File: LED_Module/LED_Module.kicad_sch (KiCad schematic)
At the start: 41 parts, among them J1 Conn_02x05_Odd_Even, J2 Conn_01x03_Male, J3 ESP8266 Header, SW1 SW_Push, SW2 SW_Push, U1 LD1117S33TR_SOT223, U2 STM32F091RCTx, U3 TPS62A02DRL, U4 24AA32AF EEPROM

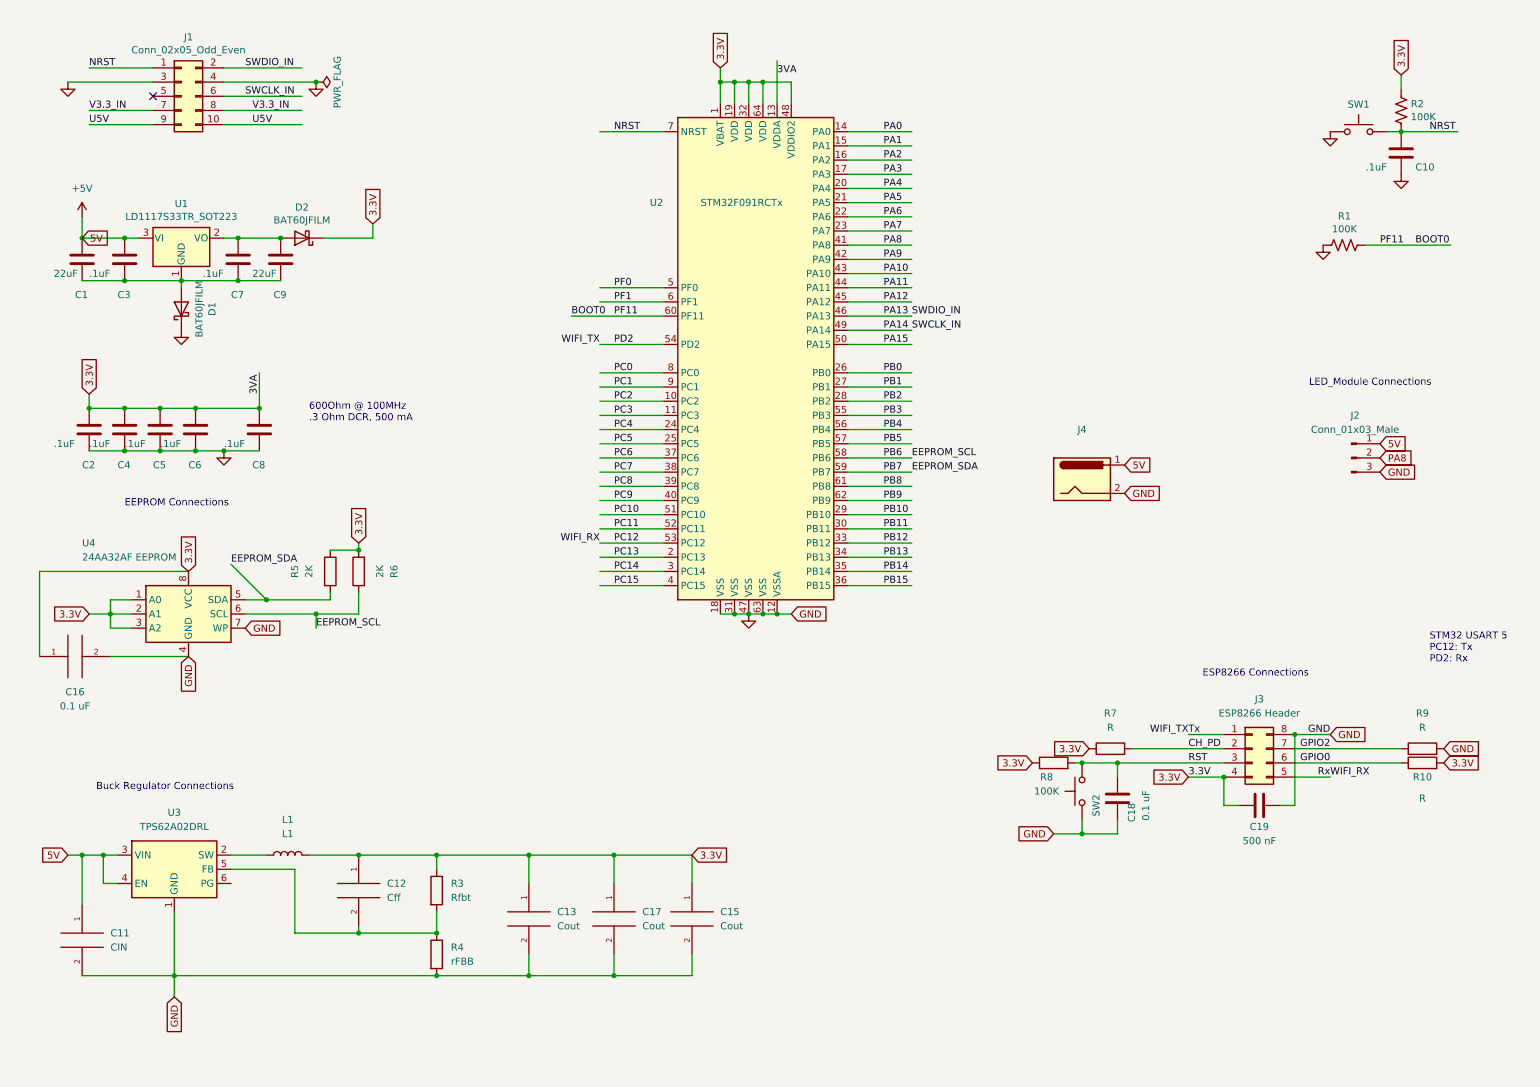
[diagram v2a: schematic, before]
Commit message: Revision to Buck Layout
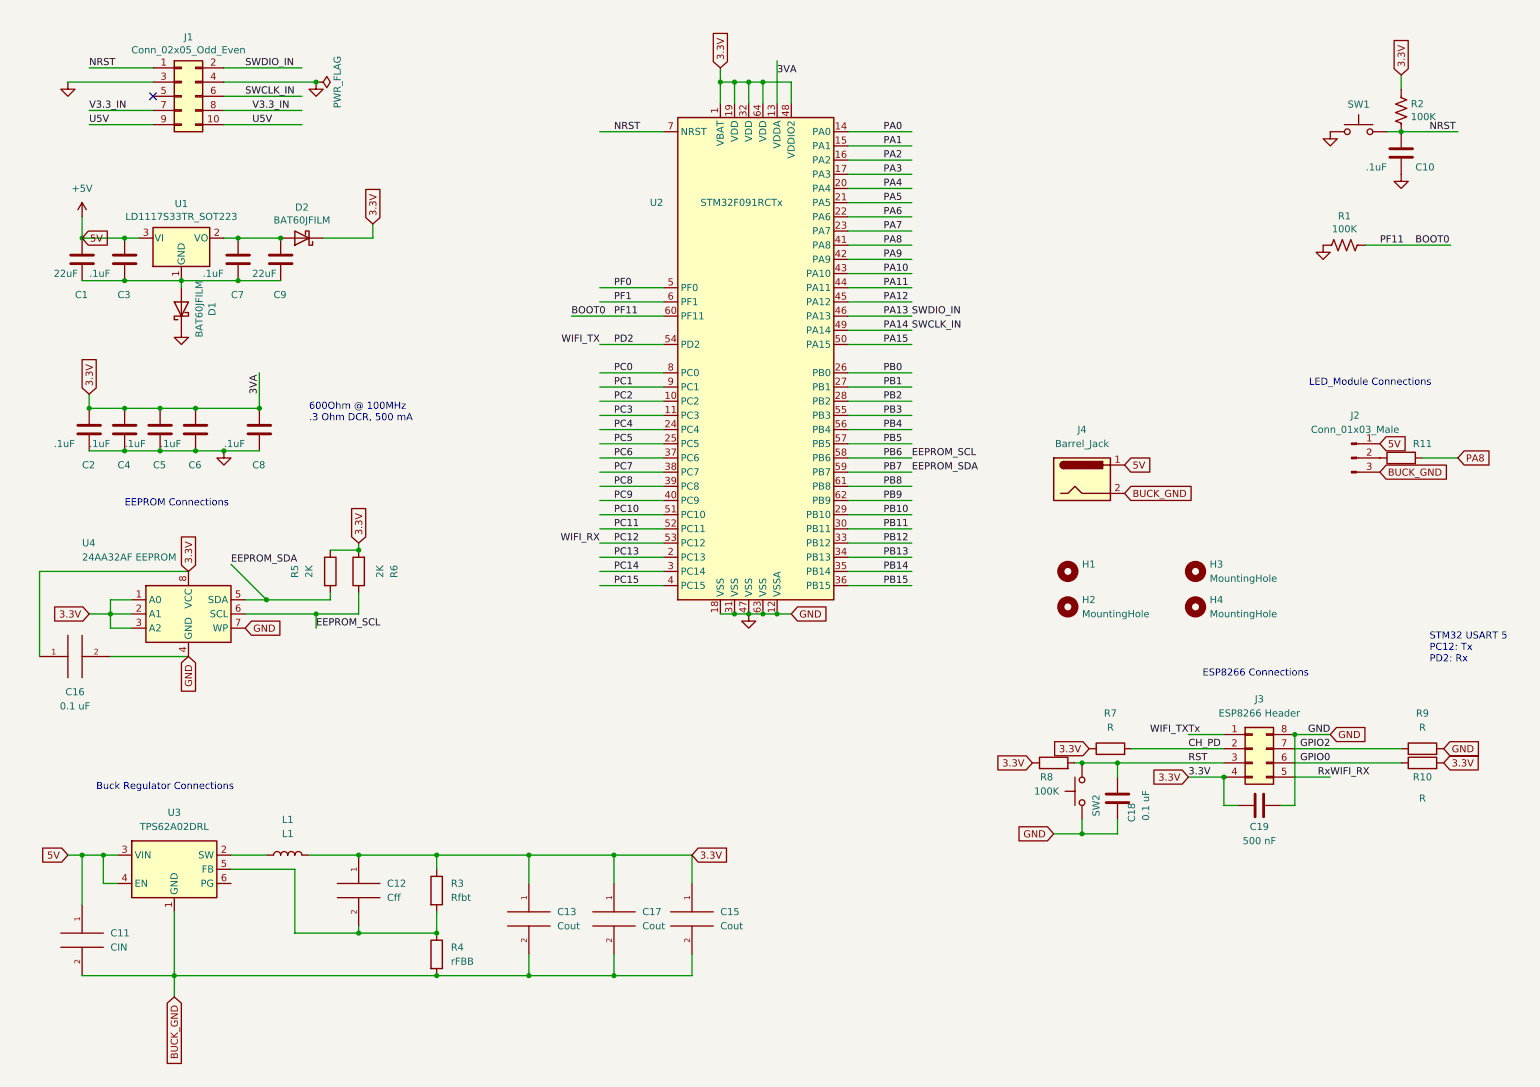
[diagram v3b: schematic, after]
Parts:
- added H1: (no value), symbol Mechanical:MountingHole
- added H2, H4: MountingHole, MountingHole:MountingHole_3.2mm_M3, symbol Mechanical:MountingHole
- added H3: MountingHole, symbol Mechanical:MountingHole
- added R11: (no value), symbol Device:R
- J4: value (none) -> Barrel_Jack; footprint (none) -> Connector_PinHeader_2.54mm:PinHeader_1x02_P2.54mm_Vertical
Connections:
- net GND: no longer C11.2, C13.2, C15.2, C17.2, J2.3 (Pin_3), J4.2, R4.2, U3.1 (GND)
- net PA8: now also R11.2; no longer J2.2 (Pin_2)
- new net: J2.2 (Pin_2), R11.1
- new net BUCK_GND: C11.2, C13.2, C15.2, C17.2, J2.3 (Pin_3), J4.2, R4.2, U3.1 (GND)
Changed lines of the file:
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@@
+    (stroke (width 0) (type default) (color 0 0 0 0))
+  )
+  (wire (pts (xy 265.43 92.71) (xy 271.78 92.71))
     (stroke (width 0) (type default) (color 0 0 0 0))
   )
@@
     )
   )
-  (global_label "PA8" (shape input) (at 257.81 92.71 0) (fields_autoplaced)
-    (effects (font (size 1.27 1.27)) (justify left))
-    (property "Intersheet References" "${INTERSHEET_REFS}" (id 0) (at 263.7912 92.6306 0)
+  (global_label "PA8" (shape input) (at 271.78 92.71 0) (fields_autoplaced)
+    (effects (font (size 1.27 1.27)) (justify left))
+    (property "Intersheet References" "${INTERSHEET_REFS}" (id 0) (at 277.7612 92.6306 0)
       (effects (font (size 1.27 1.27)) (justify left) hide)
     )
@@
     )
   )
-  (global_label "GND" (shape input) (at 212.09 99.06 0) (fields_autoplaced)
-    (effects (font (size 1.27 1.27)) (justify left))
-    (property "Intersheet References" "${INTERSHEET_REFS}" (id 0) (at 218.3736 98.9806 0)
+  (global_label "BUCK_GND" (shape input) (at 212.09 99.06 0) (fields_autoplaced)
+    (effects (font (size 1.27 1.27)) (justify left))
+    (property "Intersheet References" "${INTERSHEET_REFS}" (id 0) (at 224.4817 98.9806 0)
       (effects (font (size 1.27 1.27)) (justify left) hide)
     )
@@
     )
   )
-  (global_label "GND" (shape input) (at 41.91 189.23 270) (fields_autoplaced)
+  (global_label "BUCK_GND" (shape input) (at 41.91 189.23 270) (fields_autoplaced)
     (effects (font (size 1.27 1.27)) (justify right))
-    (property "Intersheet References" "${INTERSHEET_REFS}" (id 0) (at 41.9894 195.5136 90)
-      (effects (font (size 1.27 1.27)) (justify left) hide)
+    (property "Intersheet References" "${INTERSHEET_REFS}" (id 0) (at 41.8306 201.6217 90)
+      (effects (font (size 1.27 1.27)) (justify right) hide)
     )
   )
@@
     )
   )
-  (global_label "GND" (shape input) (at 257.81 95.25 0) (fields_autoplaced)
-    (effects (font (size 1.27 1.27)) (justify left))
-    (property "Intersheet References" "${INTERSHEET_REFS}" (id 0) (at 264.0936 95.1706 0)
+  (global_label "BUCK_GND" (shape input) (at 257.81 95.25 0) (fields_autoplaced)
+    (effects (font (size 1.27 1.27)) (justify left))
+    (property "Intersheet References" "${INTERSHEET_REFS}" (id 0) (at 270.2017 95.1706 0)
       (effects (font (size 1.27 1.27)) (justify left) hide)
     )
@@
     (pin "2")
   )
+  (symbol (lib_id "Mechanical:MountingHole") (at 224.79 119.38 0) (unit 1)
+    (in_bom yes) (on_board yes) (fields_autoplaced)
+    (property "Reference" "H4" (id 0) (at 227.33 118.1099 0)
+      (effects (font (size 1.27 1.27)) (justify left))
+    )
+    (property "Value" "MountingHole" (id 1) (at 227.33 120.6499 0)
+      (effects (font (size 1.27 1.27)) (justify left))
+    )
+    (property "Footprint" "MountingHole:MountingHole_3.2mm_M3" (id 2) (at 224.79 119.38 0)
+      (effects (font (size 1.27 1.27)) hide)
+    )
+    (property "Datasheet" "~" (id 3) (at 224.79 119.38 0)
+      (effects (font (size 1.27 1.27)) hide)
+    )
+  )
   (symbol (lib_id "Device:C") (at 26.67 87.63 0) (unit 1)
     (in_bom yes) (on_board yes)
@@
     (pin "2")
   )
+  (symbol (lib_id "Mechanical:MountingHole") (at 201.93 119.38 0) (unit 1)
+    (in_bom yes) (on_board yes) (fields_autoplaced)
+    (property "Reference" "H2" (id 0) (at 204.47 118.1099 0)
+      (effects (font (size 1.27 1.27)) (justify left))
+    )
+    (property "Value" "MountingHole" (id 1) (at 204.47 120.6499 0)
+      (effects (font (size 1.27 1.27)) (justify left))
+    )
+    (property "Footprint" "MountingHole:MountingHole_3.2mm_M3" (id 2) (at 201.93 119.38 0)
+      (effects (font (size 1.27 1.27)) hide)
+    )
+    (property "Datasheet" "~" (id 3) (at 201.93 119.38 0)
+      (effects (font (size 1.27 1.27)) hide)
+    )
+  )
   (symbol (lib_id "power:GND") (at 43.18 69.85 0) (unit 1)
     (in_bom yes) (on_board yes)
@@
     (pin "1")
   )
+  (symbol (lib_id "Mechanical:MountingHole") (at 201.93 113.03 0) (unit 1)
+    (in_bom yes) (on_board yes) (fields_autoplaced)
+    (property "Reference" "H1" (id 0) (at 204.47 111.7599 0)
+      (effects (font (size 1.27 1.27)) (justify left))
+    )
+    (property "Value" "" (id 1) (at 204.47 114.2999 0)
+      (effects (font (size 1.27 1.27)) (justify left))
+    )
+    (property "Footprint" "" (id 2) (at 201.93 113.03 0)
+      (effects (font (size 1.27 1.27)) hide)
+    )
+    (property "Datasheet" "~" (id 3) (at 201.93 113.03 0)
+      (effects (font (size 1.27 1.27)) hide)
+    )
+  )
   (symbol (lib_id "pspice:CAP") (at 25.4 179.07 0) (unit 1)
     (in_bom yes) (on_board yes) (fields_autoplaced)
@@
     )
     (property "Datasheet" "~" (id 3) (at 88.9 181.61 0)
+      (effects (font (size 1.27 1.27)) hide)
+    )
+    (pin "1")
+    (pin "2")
+  )
+  (symbol (lib_id "Device:R") (at 261.62 92.71 90) (unit 1)
+    (in_bom yes) (on_board yes)
+    (property "Reference" "R11" (id 0) (at 265.43 90.17 90))
+    (property "Value" "" (id 1) (at 265.43 92.71 90))
+    (property "Footprint" "" (id 2) (at 261.62 94.488 90)
+      (effects (font (size 1.27 1.27)) hide)
+    )
+    (property "Datasheet" "~" (id 3) (at 261.62 92.71 0)
       (effects (font (size 1.27 1.27)) hide)
     )
@@
     (pin "1")
   )
+  (symbol (lib_id "Mechanical:MountingHole") (at 224.79 113.03 0) (unit 1)
+    (in_bom yes) (on_board yes) (fields_autoplaced)
+    (property "Reference" "H3" (id 0) (at 227.33 111.7599 0)
+      (effects (font (size 1.27 1.27)) (justify left))
+    )
+    (property "Value" "MountingHole" (id 1) (at 227.33 114.2999 0)
+      (effects (font (size 1.27 1.27)) (justify left))
+    )
+    (property "Footprint" "" (id 2) (at 224.79 113.03 0)
+      (effects (font (size 1.27 1.27)) hide)
+    )
+    (property "Datasheet" "~" (id 3) (at 224.79 113.03 0)
+      (effects (font (size 1.27 1.27)) hide)
+    )
+  )
   (symbol (lib_id "pspice:CAP") (at 24.13 128.27 90) (unit 1)
     (in_bom yes) (on_board yes)
@@
     (in_bom yes) (on_board yes) (fields_autoplaced)
     (property "Reference" "J4" (id 0) (at 204.47 87.63 0))
-    (property "Value" "" (id 1) (at 204.47 90.17 0))
-    (property "Footprint" "" (id 2) (at 205.74 97.536 0)
+    (property "Value" "Barrel_Jack" (id 1) (at 204.47 90.17 0))
+    (property "Footprint" "Connector_PinHeader_2.54mm:PinHeader_1x02_P2.54mm_Vertical" (id 2) (at 205.74 97.536 0)
       (effects (font (size 1.27 1.27)) hide)
     )
@@
       (reference "D2") (unit 1) (value "BAT60JFILM") (footprint "Diode_SMD:D_SOD-323")
     )
+    (path "/6db4c715-f604-4ad5-b3e6-77e085153a04"
+      (reference "H1") (unit 1) (value "MountingHole") (footprint "MountingHole:MountingHole_3.2mm_M3")
+    )
+    (path "/622b77b6-409c-43f6-9eed-dd8b04a79249"
+      (reference "H2") (unit 1) (value "MountingHole") (footprint "MountingHole:MountingHole_3.2mm_M3")
+    )
+    (path "/d204374d-427d-4184-8cac-34c3c45ae776"
+      (reference "H3") (unit 1) (value "MountingHole") (footprint "MountingHole:MountingHole_3.2mm_M3")
+    )
+    (path "/59398cac-fd77-444e-9c8c-50373aefc347"
+      (reference "H4") (unit 1) (value "MountingHole") (footprint "MountingHole:MountingHole_3.2mm_M3")
+    )
     (path "/c7c34d7a-e4e9-4020-9eb2-3f57bf5616f3"
       (reference "J1") (unit 1) (value "Conn_02x05_Odd_Even") (footprint "Connector_IDC:IDC-Header_2x05_P2.54mm_Vertical")
@@
       (reference "R10") (unit 1) (value "R") (footprint "Resistor_SMD:R_0805_2012Metric_Pad1.20x1.40mm_HandSolder")
     )
+    (path "/76abd028-2505-456e-9c1d-86a704fa9431"
+      (reference "R11") (unit 1) (value "R") (footprint "Resistor_SMD:R_0805_2012Metric_Pad1.20x1.40mm_HandSolder")
+    )
     (path "/83a0af08-0788-496b-b5a2-dc27514fcb3a"

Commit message: Systems laid out and 3.3V connected
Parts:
- removed R9: R, Resistor_SMD:R_0805_2012Metric_Pad1.20x1.40mm_HandSolder, symbol Device:R
- added D3, D4, D6: LED, LED_SMD:LED_0805_2012Metric_Pad1.15x1.40mm_HandSolder, symbol Device:LED
- added D5: (no value), symbol Device:LED
- added R12, R14, R9: 3K, Resistor_SMD:R_0805_2012Metric_Pad1.20x1.40mm_HandSolder, symbol Device:R_US
- added R13: (no value), symbol Device:R_US
- SW2: footprint Button_Switch_SMD:SW_SPST_PTS645 -> (none)
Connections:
- net 3.3V: now also J3.7 (3.3V); no longer J3.4 (3.3V)
- net CH_PD: now also J3.3 (CH_PD); no longer J3.2 (CH_PD)
- net GND: now also J3.2 (GND), D3.1 (K), D4.1 (K), D5.1 (K), D6.1 (K); no longer J3.8 (GND)
- net GPIO2: no longer J3.7 (GPIO2)
- net PC12: now also J3.8 (Rx); no longer J3.5 (Rx)
- net PC6: now also R9.2
- net PC7: now also R12.2
- net PC8: now also R13.2
- net PC9: now also R14.2
- net RST: now also J3.5 (RST); no longer J3.3 (RST)
- new net: D6.2 (A), R14.1
- new net: D5.2 (A), R13.1
- new net: D3.2 (A), R9.1
- new net: D4.2 (A), R12.1
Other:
- moved on the sheet: J2, R11

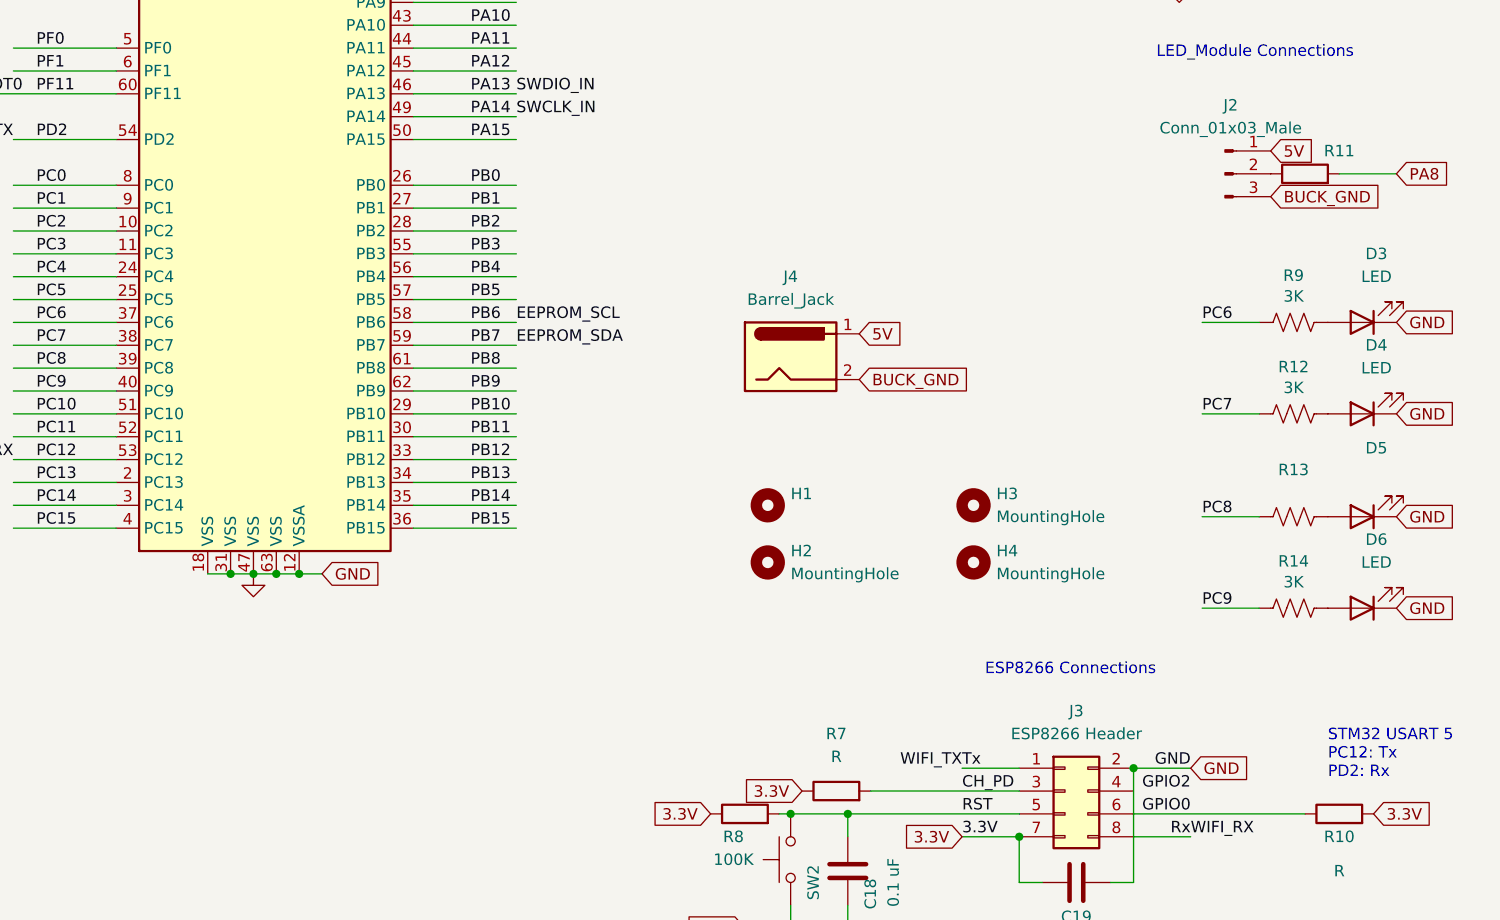
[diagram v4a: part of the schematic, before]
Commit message: Power and ground planes plus complete routing
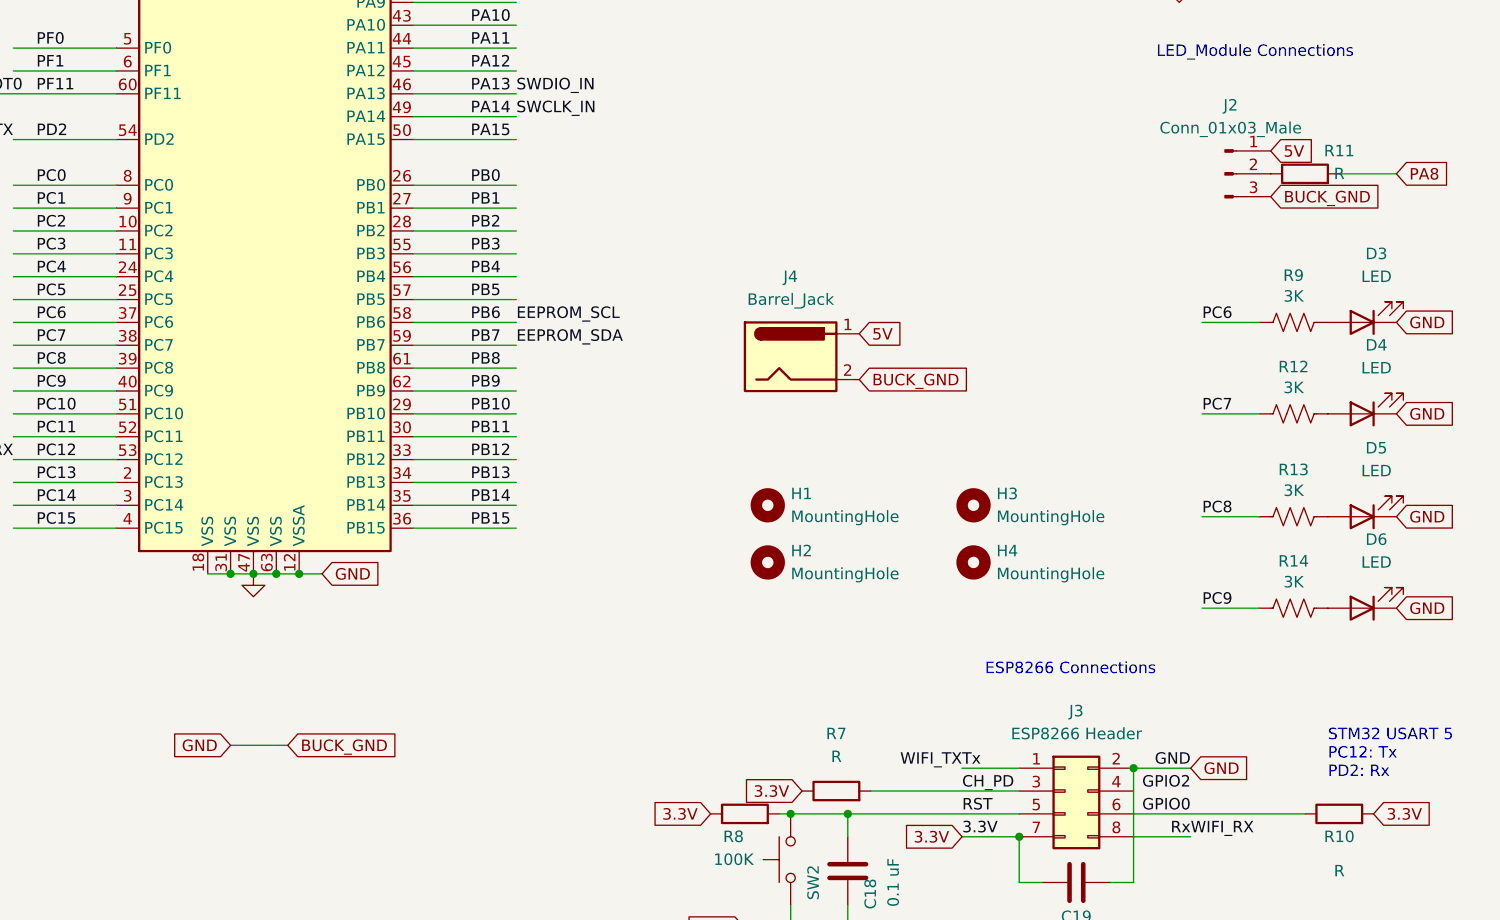
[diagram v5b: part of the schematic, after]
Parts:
- D3, D4, D6: footprint LED_SMD:LED_0805_2012Metric_Pad1.15x1.40mm_HandSolder -> (none)
- D5: value (none) -> LED
- H1: value (none) -> MountingHole; footprint (none) -> MountingHole:MountingHole_3.2mm_M3
- H3: footprint (none) -> MountingHole:MountingHole_3.2mm_M3
- R11: value (none) -> R; footprint (none) -> Resistor_SMD:R_0805_2012Metric_Pad1.20x1.40mm_HandSolder
- R12, R14, R9: footprint Resistor_SMD:R_0805_2012Metric_Pad1.20x1.40mm_HandSolder -> (none)
- R13: value (none) -> 3K
- SW2: footprint (none) -> Button_Switch_SMD:SW_SPST_PTS645
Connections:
- net BUCK_GND is gone; now on net GND: C11.2, C13.2, C15.2, C17.2, J2.3 (Pin_3), J4.2, R4.2, U3.1 (GND)
